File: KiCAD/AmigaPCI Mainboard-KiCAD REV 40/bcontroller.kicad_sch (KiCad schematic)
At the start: 32 parts, among them CN409 SPI, J901 IDE MODES, U111 74LVC16646, U112 74LVC16646, U409 ICE40HX4K-TQ144, U409F1 W25X20CLSN

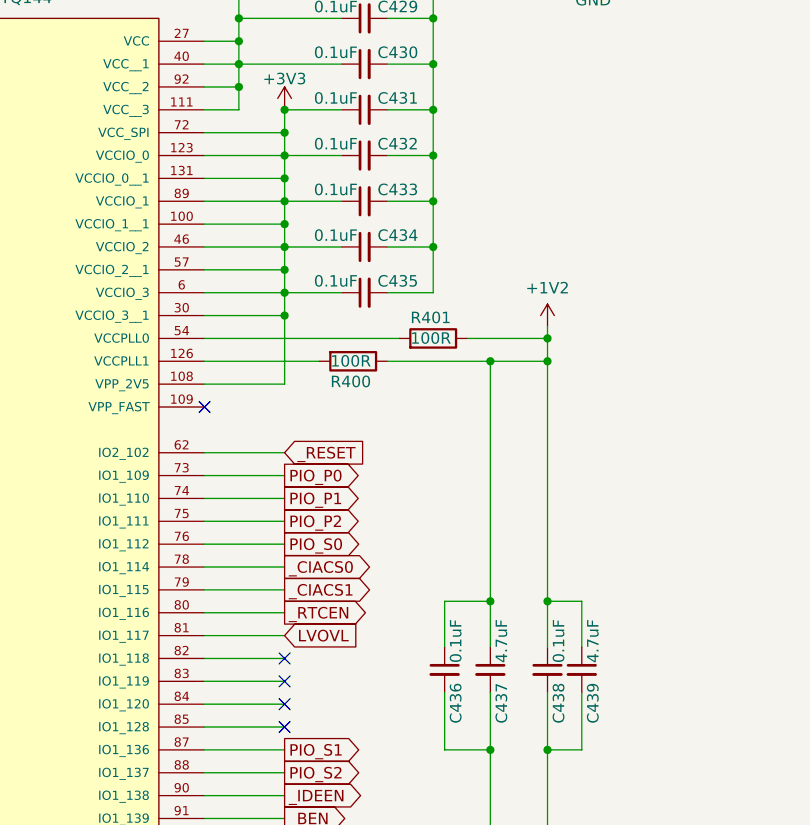
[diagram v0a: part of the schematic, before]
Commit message: Modified PLL power filters. 30-JUN-2024
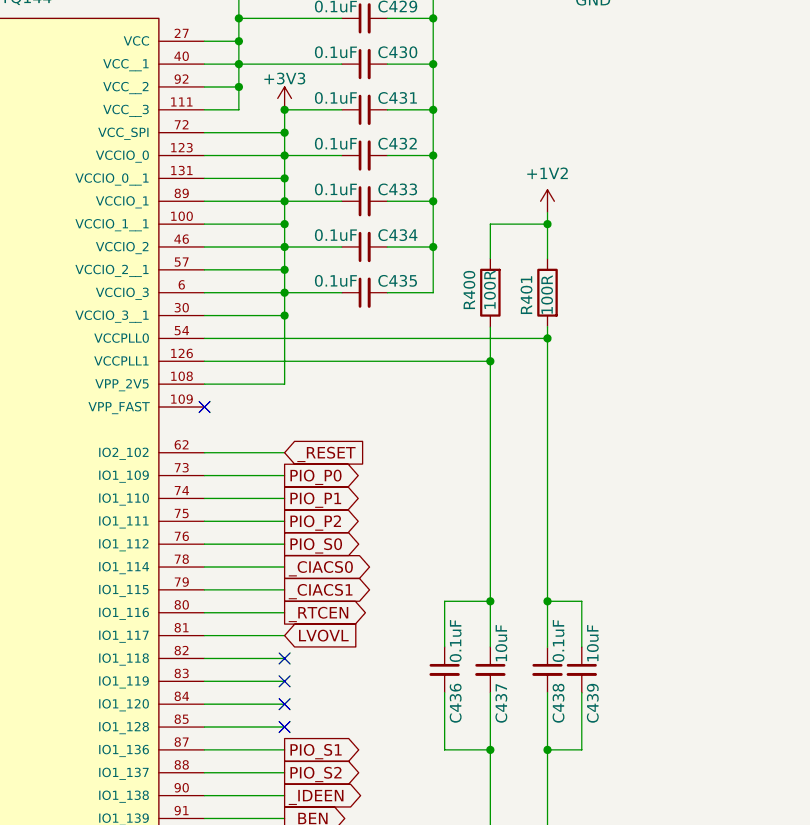
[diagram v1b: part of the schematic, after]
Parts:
- C437, C439: value 4.7uF -> 10uF
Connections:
- net +1V2: now also R400.2; no longer C436.1, C437.1, C438.1, C439.1, R400.1
- net at R401.2, U409.54 (VCCPLL0): now also C438.1, C439.1
- net at U409.126 (VCCPLL1): now also C436.1, C437.1, R400.1; no longer R400.2
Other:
- moved on the sheet: R400, R401
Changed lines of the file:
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@@
 	)
 	(junction
+		(at 176.53 81.28)
+		(diameter 0)
+		(color 0 0 0 0)
+	)
+	(junction
 		(at 378.46 200.66)
 		(diameter 0)
@@
 	)
 	(junction
-		(at 170.18 83.82)
-		(diameter 0)
-		(color 0 0 0 0)
-	)
-	(junction
 		(at 163.83 40.64)
 		(diameter 0)
@@
 	)
 	(junction
+		(at 170.18 83.82)
+		(diameter 0)
+		(color 0 0 0 0)
+	)
+	(junction
 		(at 142.24 35.56)
 		(diameter 0)
@@
 	)
 	(junction
-		(at 176.53 81.28)
+		(at 142.24 45.72)
 		(diameter 0)
 		(color 0 0 0 0)
 	)
 	(junction
-		(at 142.24 45.72)
+		(at 176.53 68.58)
 		(diameter 0)
 		(color 0 0 0 0)
@@
 	)
 	(junction
-		(at 176.53 83.82)
-		(diameter 0)
-		(color 0 0 0 0)
-	)
-	(junction
 		(at 142.24 50.8)
 		(diameter 0)
@@
 	(wire
 		(pts
-			(xy 170.18 83.82) (xy 158.75 83.82)
-		)
-		(stroke
-			(width 0)
-			(type default)
-		)
-	)
-	(wire
-		(pts
 			(xy 186.69 157.48) (xy 186.69 154.94)
 		)
@@
 	(wire
 		(pts
-			(xy 138.43 83.82) (xy 151.13 83.82)
+			(xy 138.43 83.82) (xy 170.18 83.82)
 		)
 		(stroke
@@
 	(wire
 		(pts
-			(xy 170.18 83.82) (xy 176.53 83.82)
-		)
-		(stroke
-			(width 0)
-			(type default)
-		)
-	)
-	(wire
-		(pts
 			(xy 55.88 57.15) (xy 55.88 60.96)
 		)
@@
 	(wire
 		(pts
-			(xy 176.53 80.01) (xy 176.53 81.28)
-		)
-		(stroke
-			(width 0)
-			(type default)
-		)
-	)
-	(wire
-		(pts
 			(xy 36.83 83.82) (xy 36.83 85.09)
 		)
@@
 	(wire
 		(pts
+			(xy 170.18 68.58) (xy 176.53 68.58)
+		)
+		(stroke
+			(width 0)
+			(type default)
+		)
+	)
+	(wire
+		(pts
 			(xy 81.28 220.98) (xy 81.28 223.52)
 		)
@@
 		)
 	)
+	(wire
+		(pts
+			(xy 176.53 81.28) (xy 176.53 110.49)
+		)
+		(stroke
+			(width 0)
+			(type default)
+		)
+	)
 	(bus
 		(pts
@@
 	(wire
 		(pts
-			(xy 170.18 110.49) (xy 170.18 83.82)
+			(xy 170.18 80.01) (xy 170.18 83.82)
 		)
 		(stroke
@@
 		)
 	)
+	(wire
+		(pts
+			(xy 170.18 83.82) (xy 170.18 110.49)
+		)
+		(stroke
+			(width 0)
+			(type default)
+		)
+	)
 	(bus
 		(pts
@@
 	(wire
 		(pts
+			(xy 170.18 72.39) (xy 170.18 68.58)
+		)
+		(stroke
+			(width 0)
+			(type default)
+		)
+	)
+	(wire
+		(pts
 			(xy 147.32 132.08) (xy 138.43 132.08)
 		)
@@
 	(wire
 		(pts
-			(xy 176.53 81.28) (xy 167.64 81.28)
-		)
-		(stroke
-			(width 0)
-			(type default)
-		)
-	)
-	(wire
-		(pts
 			(xy 395 109.22) (xy 383.57 109.22)
 		)
@@
 	(wire
 		(pts
+			(xy 176.53 68.58) (xy 176.53 72.39)
+		)
+		(stroke
+			(width 0)
+			(type default)
+		)
+	)
+	(wire
+		(pts
 			(xy 53.34 63.5) (xy 87.63 63.5)
 		)
@@
 	(wire
 		(pts
-			(xy 176.53 83.82) (xy 176.53 110.49)
+			(xy 176.53 80.01) (xy 176.53 81.28)
 		)
 		(stroke
@@
 	(wire
 		(pts
+			(xy 176.53 67.31) (xy 176.53 68.58)
+		)
+		(stroke
+			(width 0)
+			(type default)
+		)
+	)
+	(wire
+		(pts
 			(xy 138.43 96.52) (xy 147.32 96.52)
 		)
@@
 		)
 	)
-	(wire
-		(pts
-			(xy 176.53 81.28) (xy 176.53 83.82)
-		)
-		(stroke
-			(width 0)
-			(type default)
-		)
-	)
 	(bus
 		(pts
@@
 	(wire
 		(pts
-			(xy 138.43 81.28) (xy 160.02 81.28)
+			(xy 138.43 81.28) (xy 176.53 81.28)
 		)
 		(stroke
@@
 	(symbol
 		(lib_id "power:+1V2")
-		(at 176.53 80.01 0)
+		(at 176.53 67.31 0)
 		(unit 1)
 		(exclude_from_sim no)
@@
 		(fields_autoplaced yes)
 		(property "Reference" "#PWR024"
-			(at 176.53 83.82 0)
+			(at 176.53 71.12 0)
 			(effects
 				(font
@@
 		)
 		(property "Value" "+1V2"
-			(at 176.53 75.692 0)
+			(at 176.53 62.992 0)
 			(effects
 				(font
@@
 		)
 		(property "Footprint" ""
-			(at 176.53 80.01 0)
+			(at 176.53 67.31 0)
 			(effects
 				(font
@@
 		)
 		(property "Datasheet" ""
-			(at 176.53 80.01 0)
+			(at 176.53 67.31 0)
 			(effects
 				(font
@@
 		)
 		(property "Description" ""
-			(at 176.53 80.01 0)
+			(at 176.53 67.31 0)
 			(effects
 				(font
@@
 			)
 		)
-		(property "Value" "4.7uF"
+		(property "Value" "10uF"
 			(at 171.45 117.348 90)
 			(effects
@@
 	(symbol
 		(lib_id "Device:R")
-		(at 163.83 81.28 270)
-		(mirror x)
+		(at 176.53 76.2 0)
+		(mirror y)
 		(unit 1)
 		(exclude_from_sim no)
@@
 		(dnp no)
 		(property "Reference" "R401"
-			(at 161.29 78.994 90)
+			(at 174.244 78.74 90)
 			(effects
 				(font
@@
 		)
 		(property "Value" "100R"
-			(at 161.29 81.28 90)
+			(at 176.53 78.74 90)
 			(effects
 				(font
@@
 		)
 		(property "Footprint" "Resistor_SMD:R_0603_1608Metric"
-			(at 163.83 83.058 90)
+			(at 178.308 76.2 90)
 			(effects
 				(font
@@
 		)
 		(property "Datasheet" "~"
-			(at 163.83 81.28 0)
+			(at 176.53 76.2 0)
 			(effects
 				(font
@@
 		)
 		(property "Description" ""
-			(at 163.83 81.28 0)
+			(at 176.53 76.2 0)
 			(effects
 				(font
@@
 			)
 		)
-		(property "Value" "4.7uF"
+		(property "Value" "10uF"
 			(at 181.61 117.348 90)
 			(effects
@@
 	(symbol
 		(lib_id "Device:R")
-		(at 154.94 83.82 270)
+		(at 170.18 76.2 180)
 		(unit 1)
 		(exclude_from_sim no)
@@
 		(dnp no)
 		(property "Reference" "R400"
-			(at 152.4 86.106 90)
+			(at 167.894 73.66 90)
 			(effects
 				(font
@@
 		)
 		(property "Value" "100R"
-			(at 152.4 83.82 90)
+			(at 170.18 73.66 90)
 			(effects
 				(font
@@
 		)
 		(property "Footprint" "Resistor_SMD:R_0603_1608Metric"
-			(at 154.94 82.042 90)
+			(at 171.958 76.2 90)
 			(effects
 				(font
@@
 		)
 		(property "Datasheet" "~"
-			(at 154.94 83.82 0)
+			(at 170.18 76.2 0)
 			(effects
 				(font
@@
 		)
 		(property "Description" ""
-			(at 154.94 83.82 0)
+			(at 170.18 76.2 0)
 			(effects
 				(font

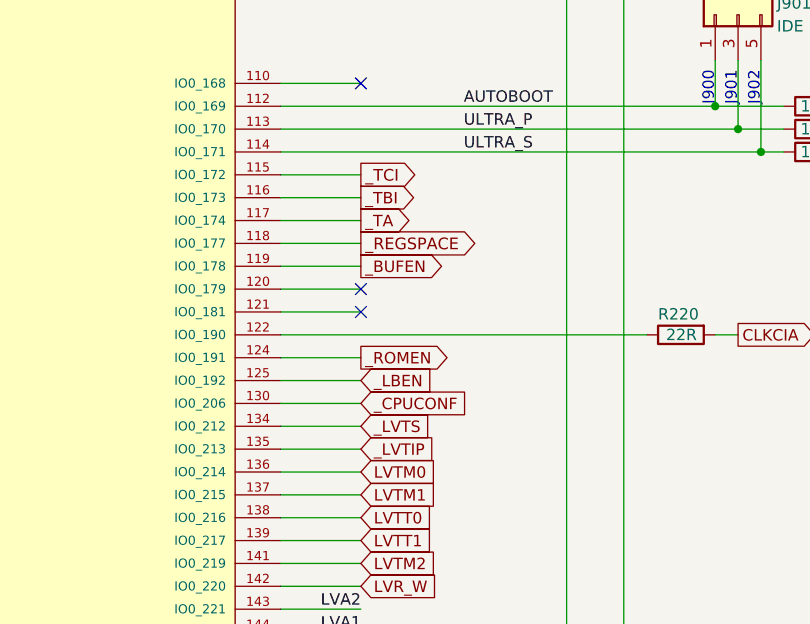
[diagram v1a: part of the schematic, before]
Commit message: Schematic Changes for Rev 4.0 03-JUL-2024
Remove _TIP, replace with GND at CN200.
Add _TS to U712.
Remove _TCI and _TBI from U409.
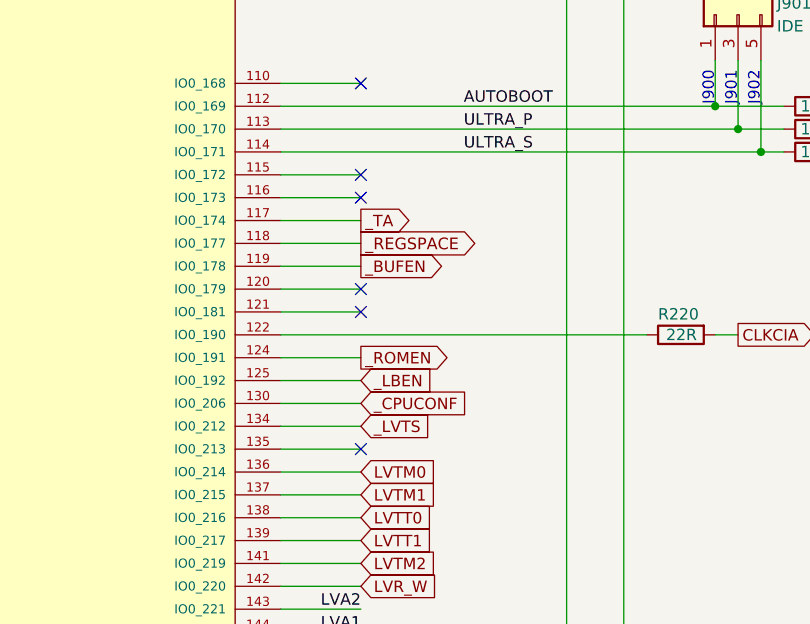
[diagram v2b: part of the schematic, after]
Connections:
- net _LVTIP: no longer names the net of U409.135 (IO0_213)
- net _TBI: no longer names the net of U409.116 (IO0_173)
- net _TCI: no longer names the net of U409.115 (IO0_172)
- no-connect marks 26 -> 29
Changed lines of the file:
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@@
 	(title_block
 		(title "AMIGA PCI")
-		(date "2024-06-29")
+		(date "2024-07-03")
 		(rev "4.0")
 	)
@@
 	)
 	(no_connect
+		(at 147.32 185.42)
+	)
+	(no_connect
 		(at 147.32 152.4)
 	)
@@
 	)
 	(no_connect
+		(at 147.32 182.88)
+	)
+	(no_connect
 		(at 147.32 142.24)
 	)
@@
 	)
 	(no_connect
+		(at 147.32 213.36)
+	)
+	(no_connect
 		(at 87.63 58.42)
 	)
@@
 		)
 	)
-	(global_label "_LVTIP"
-		(shape input)
-		(at 147.32 213.36 0)
-		(fields_autoplaced yes)
-		(effects
-			(font
-				(size 1.27 1.27)
-			)
-			(justify left)
-		)
-		(property "Intersheetrefs" "${INTERSHEET_REFS}"
-			(at 156.2319 213.36 0)
-			(effects
-				(font
-					(size 1.27 1.27)
-				)
-				(justify left)
-			)
-		)
-	)
 	(global_label "_ROMEN"
 		(shape output)
@@
 		)
 	)
-	(global_label "_TBI"
-		(shape output)
-		(at 147.32 185.42 0)
-		(fields_autoplaced yes)
-		(effects
-			(font
-				(size 1.27 1.27)
-			)
-			(justify left)
-		)
-		(property "Intersheetrefs" "${INTERSHEET_REFS}"
-			(at 154.0358 185.42 0)
-			(effects
-				(font
-					(size 1.27 1.27)
-				)
-				(justify left)
-			)
-		)
-	)
 	(global_label "PIO_S0"
 		(shape output)
@@
 			(effects
 				(font
-					(size 1.27 1.27)
-				)
-				(justify left)
-			)
-		)
-	)
-	(global_label "_TCI"
-		(shape output)
-		(at 147.32 182.88 0)
-		(fields_autoplaced yes)
-		(effects
-			(font
-				(size 1.2954 1.2954)
-			)
-			(justify left)
-		)
-		(property "Intersheetrefs" "${INTERSHEET_REFS}"
-			(at 154.2507 182.88 0)
-			(effects
-				(font
